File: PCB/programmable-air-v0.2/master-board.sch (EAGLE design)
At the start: 20 parts, among them J1 POWER_JACKTOE

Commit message: Post Rube Goldberg. Working on PCB v0.2
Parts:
- removed J4: (no value), SparkFun-Connectors:CONN_08"
- added D1, D2: (no value), SparkFun-LED:LED0603
- added R3, R4: 4.7k, SparkFun-Resistors:4.7KOHM-0603-1/10W-1%
- added S1, S2: MOMENTARY-SWITCH-SPST-SMD-5.2MM, SparkFun-Switches:MOMENTARY-SWITCH-SPST-SMD-5.2MM
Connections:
- removed net N$29: ARDUINO_NANO1.ADC0/A0, J5.4
- new net GGRID: D1.A, U$1.P$1, U$3.P$1
- new net N$12: D1.C, R3.1
- new net N$17: D2.C, R4.1
- net GND: no longer J4.8
- net N$10: now also ARDUINO_NANO1.D12/MISO; no longer ARDUINO_NANO1.ADC3/A3
- net N$11: now also ARDUINO_NANO1.ADC1/A1, J5.4; no longer ARDUINO_NANO1.ADC4/SDA/A4, J4.6
- net N$13: no longer J4.5
- net N$14: now also ARDUINO_NANO1.ADC0/A0; no longer ARDUINO_NANO1.ADC6/A6
- net N$15: now also ARDUINO_NANO1.D2/INT0; no longer ARDUINO_NANO1.ADC7/A7
- net N$16: now also ARDUINO_NANO1.ADC5/SCL/A5; no longer ARDUINO_NANO1.D2/INT0, J4.2
- net N$18: now also ARDUINO_NANO1.ADC4/SDA/A4; no longer ARDUINO_NANO1.D12/MISO, J4.4
- net N$20: no longer J4.7
- net N$27: now also ARDUINO_NANO1.ADC3/A3; no longer ARDUINO_NANO1.ADC2/A2
- net N$28: now also ARDUINO_NANO1.ADC2/A2; no longer ARDUINO_NANO1.ADC1/A1
- net N$5: now also R3.2
- net N$6: now also R4.2
- net N$8: no longer J4.3
- net VIN: now also D2.A; no longer J4.1, U$1.P$1, U$3.P$1

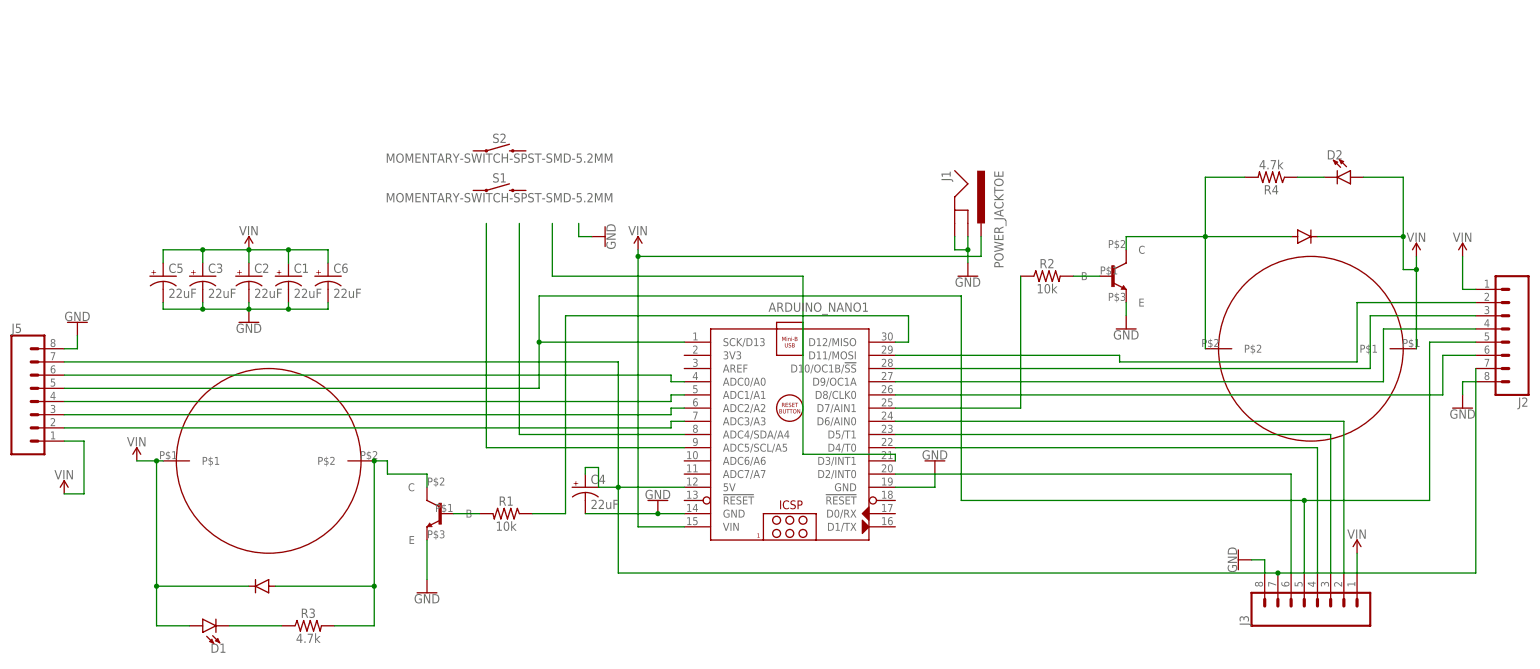
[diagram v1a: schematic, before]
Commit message: Master PCB v0.2 schematic and positioning complee. Going to start routing
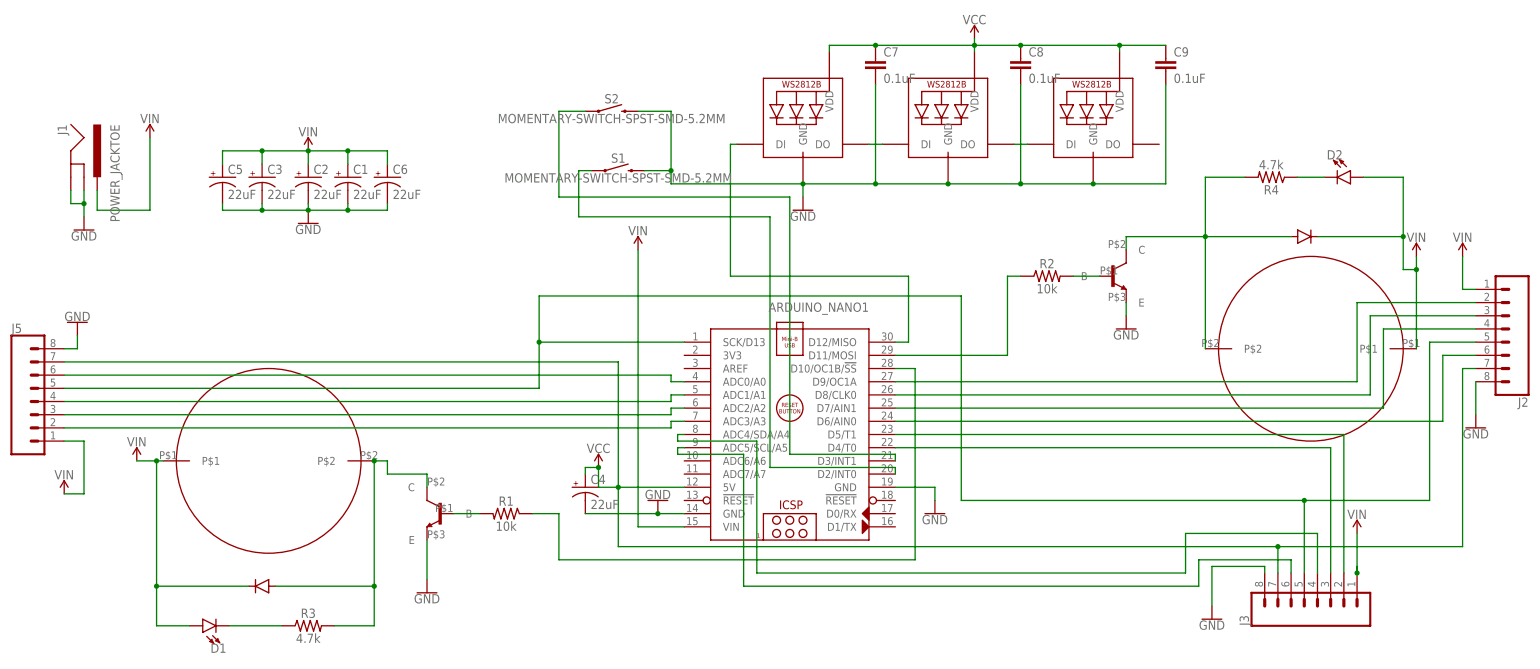
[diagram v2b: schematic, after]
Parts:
- added C7, C8, C9: 0.1uF, SparkFun-Capacitors:0.1UF-0603-25V-(+80/-20%)
- added LED1, LED2, LED3: WS2812B5050, adafruit:WS2812B5050
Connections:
- removed net GGRID: D1.A, U$1.P$1, U$3.P$1
- removed net N$16: ARDUINO_NANO1.ADC5/SCL/A5
- removed net N$18: ARDUINO_NANO1.ADC4/SDA/A4
- removed net N$20: ARDUINO_NANO1.5V, C4.+, J2.7, J3.7, J5.7
- new net N$19: ARDUINO_NANO1.D2/INT0, S1.1
- new net N$21: LED2.DO, LED3.DI
- new net N$26: LED1.DO, LED2.DI
- new net N$29: ARDUINO_NANO1.D3/INT1, S2.1
- new net VCC: ARDUINO_NANO1.5V, C4.+, C7.1, C8.1, C9.1, J2.7, J3.7, J5.7, LED1.VDD, LED2.VDD, LED3.VDD
- net GND: now also C7.2, C8.2, C9.2, LED1.GND, LED2.GND, LED3.GND, S1.2, S2.2
- net N$1: now also ARDUINO_NANO1.D11/MOSI; no longer ARDUINO_NANO1.D7/AIN1
- net N$10: now also ARDUINO_NANO1.D10/OC1B/!SS; no longer ARDUINO_NANO1.D12/MISO
- net N$15: now also ARDUINO_NANO1.ADC5/SCL/A5; no longer ARDUINO_NANO1.D2/INT0
- net N$22: now also ARDUINO_NANO1.D6/AIN0; no longer ARDUINO_NANO1.D8/CLK0
- net N$23: now also ARDUINO_NANO1.D7/AIN1; no longer ARDUINO_NANO1.D9/OC1A
- net N$24: now also ARDUINO_NANO1.D8/CLK0; no longer ARDUINO_NANO1.D10/OC1B/!SS
- net N$25: now also ARDUINO_NANO1.D9/OC1A; no longer ARDUINO_NANO1.D11/MOSI
- net N$3: now also ARDUINO_NANO1.D5/T1, J3.2; no longer ARDUINO_NANO1.D4/T0, J3.4
- net N$4: now also ARDUINO_NANO1.D4/T0; no longer ARDUINO_NANO1.D5/T1
- net N$8: now also ARDUINO_NANO1.D12/MISO, LED1.DI; no longer ARDUINO_NANO1.D3/INT1
- net N$9: now also ARDUINO_NANO1.ADC4/SDA/A4, J3.4; no longer ARDUINO_NANO1.D6/AIN0, J3.2
- net VIN: now also D1.A, U$1.P$1, U$3.P$1
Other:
- moved on the sheet: C1, C2, C3, C5, C6, J1, S1, S2

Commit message: Master PCB v0.2 routing complete
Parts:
- removed S1, S2: MOMENTARY-SWITCH-SPST-SMD-5.2MM, SparkFun-Switches:MOMENTARY-SWITCH-SPST-SMD-5.2MM
- added S3, S4: (no value), SparkFun-Switches:MOMENTARY-SWITCH-SPST-2-SMD-4.6X2.8MM
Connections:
- removed net N$19: ARDUINO_NANO1.D2/INT0, S1.1
- removed net N$27: ARDUINO_NANO1.ADC3/A3, J5.2
- removed net N$28: ARDUINO_NANO1.ADC2/A2, J5.3
- new net N$16: ARDUINO_NANO1.ADC0/A0, J5.2
- new net N$18: ARDUINO_NANO1.ADC2/A2, J5.4
- new net N$20: ARDUINO_NANO1.D2/INT0, S4.1, S4.2
- net GND: now also S3.3, S3.4, S4.3, S4.4; no longer S1.2, S2.2
- net N$11: now also J5.3; no longer J5.4
- net N$14: now also ARDUINO_NANO1.ADC3/A3; no longer ARDUINO_NANO1.ADC0/A0
- net N$29: now also S3.1, S3.2; no longer S2.1
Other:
- moved on the sheet: J5
